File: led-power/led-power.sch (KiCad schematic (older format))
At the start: 97 parts, among them J1 String1, J10 PowerInput, J11 Qwiic, J12 Qwiic, J13 A0, J14 A1, J15 A2, J2 String2, J3 String3, J4 String4, J5 String5, J6 String6, J7 String7, J8 String8, J9 PowerInput, Q1 Q_NMOS_GDS, Q2 Q_NMOS_GDS, Q3 Q_NMOS_GDS, Q4 Q_NMOS_GDS, Q5 Q_NMOS_GDS, Q6 Q_NMOS_GDS, Q7 Q_NMOS_GDS, Q8 Q_NMOS_GDS, U1 MCP6V51, U10 L78L05ACZ-AP, U11 MCP1501, U2 MCP6V51, U3 MCP6V51, U4 MCP6V51, U5 MCP6V51, U6 MCP6V51, U7 MCP6V51, U8 MCP6V51, U9 MCP23017_SO

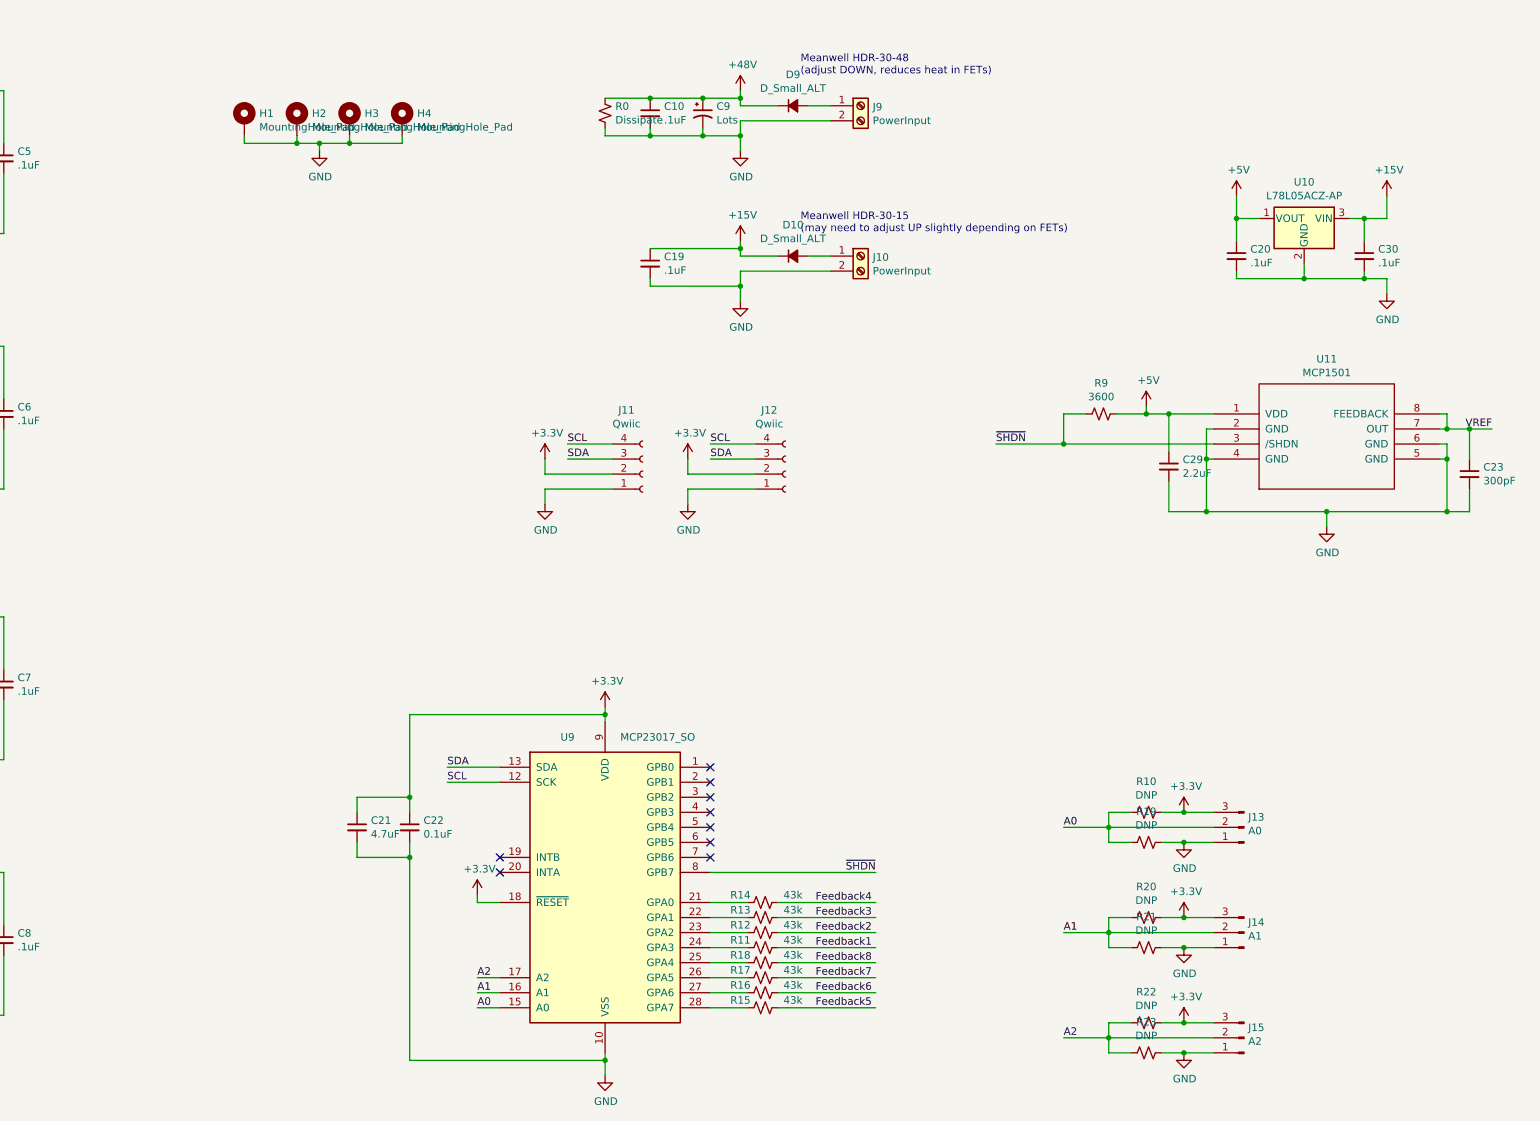
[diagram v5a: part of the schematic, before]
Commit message: Rev 2 changes
* Pulldown on VREF so that ~SHDN can work
* Voltage dividers on the rails, fed to the MCP23017 so it can detect faults
* Increased space between Qwiic headers
* Bring I2C bus out on 0.100" header
* Tweaked LED positions on the left side; right seemed to be fine.
* Converted it to a four layer board. +15V/GND/GND/+48V
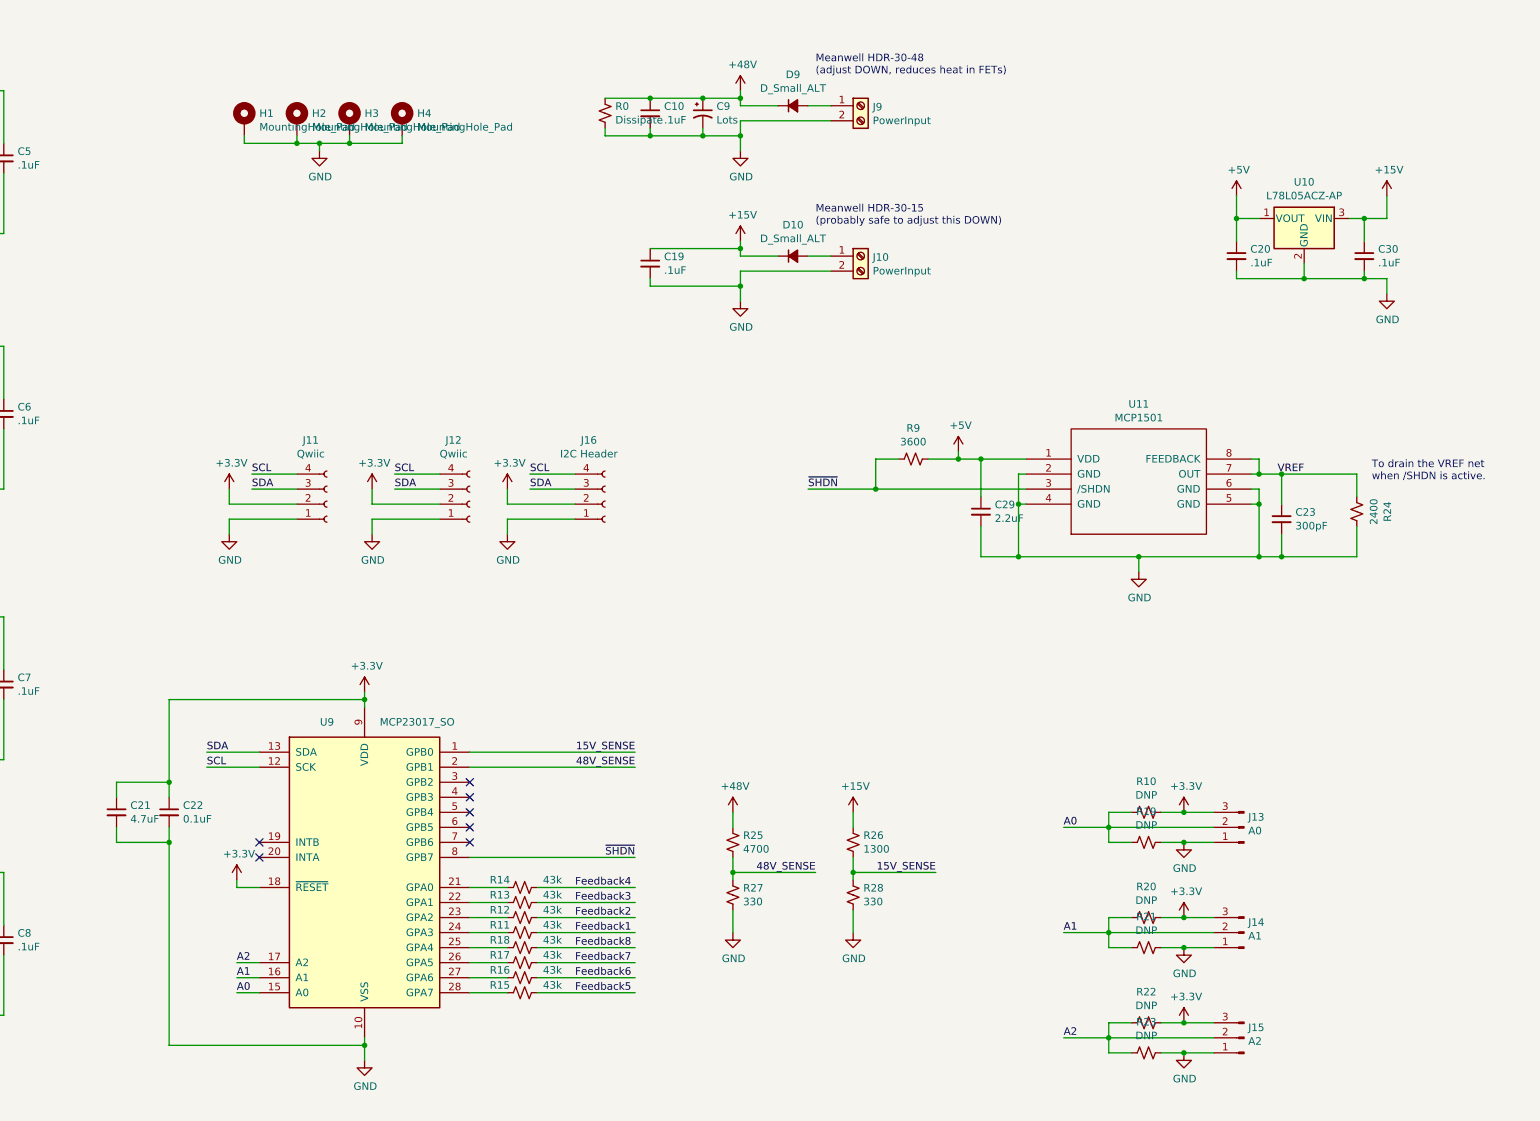
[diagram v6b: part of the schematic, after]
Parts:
- added J16: I2C Header, Pin_Headers:Pin_Header_Straight_1x04_Pitch2.54mm, symbol Connector:Conn_01x04_Female
- added R24: 2400, Resistors_SMD:R_0805_HandSoldering, symbol Device:R_Small_US
- added R25: 4700, Resistors_SMD:R_0805_HandSoldering, symbol Device:R_Small_US
- added R26: 1300, Resistors_SMD:R_0805_HandSoldering, symbol Device:R_Small_US
- added R27, R28: 330, Resistors_SMD:R_0805_HandSoldering, symbol Device:R_Small_US
- H1, H2, H3, H4: footprint Mounting_Holes:MountingHole_3.2mm_M3_Pad -> Mounting_Holes:MountingHole_3.2mm_M3_Pad_Via
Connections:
- net +15V: now also R26.1
- net +3V3: now also J16.2 (Pin_2)
- net +48V: now also R25.1
- net GND: now also J16.1 (Pin_1), R24.1, R27.2, R28.2
- net SCL: now also J16.4 (Pin_4)
- net SDA: now also J16.3 (Pin_3)
- net VREF: now also R24.2
- net 15V_SENSE: now reaches U9.1 (GPB0)
- net 15V_SENSE: now also R26.2, R28.1
- net 48V_SENSE: now reaches U9.2 (GPB1)
- net 48V_SENSE: now also R25.2, R27.1
- no-connect marks 9 -> 7
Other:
- note added: "Meanwell HDR-30-15\n(probably safe to adjust this DOWN)"
- note added: "To drain the VREF net\nwhen /SHDN is active."
- note removed: "Meanwell HDR-30-15\n(may need to adjust UP slightly depending on FETs)"
- moved on the sheet: C21, C22, C23, C29, J11, J12, R11, R12, R13, R14, R15, R16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

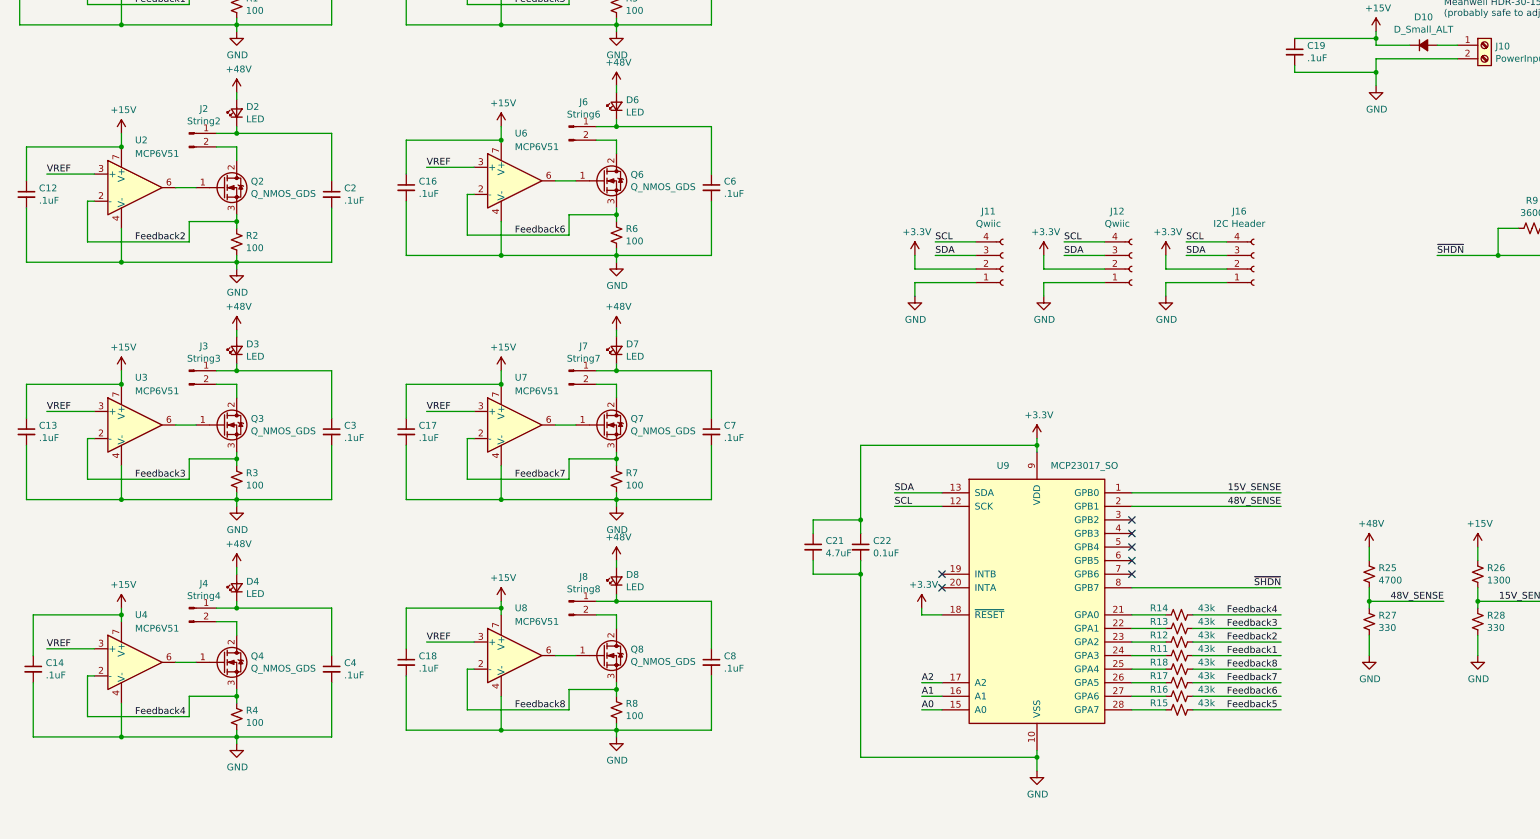
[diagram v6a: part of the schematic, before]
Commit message: Add ~IRQ header, lots of trace cleanup. Bump the board rev
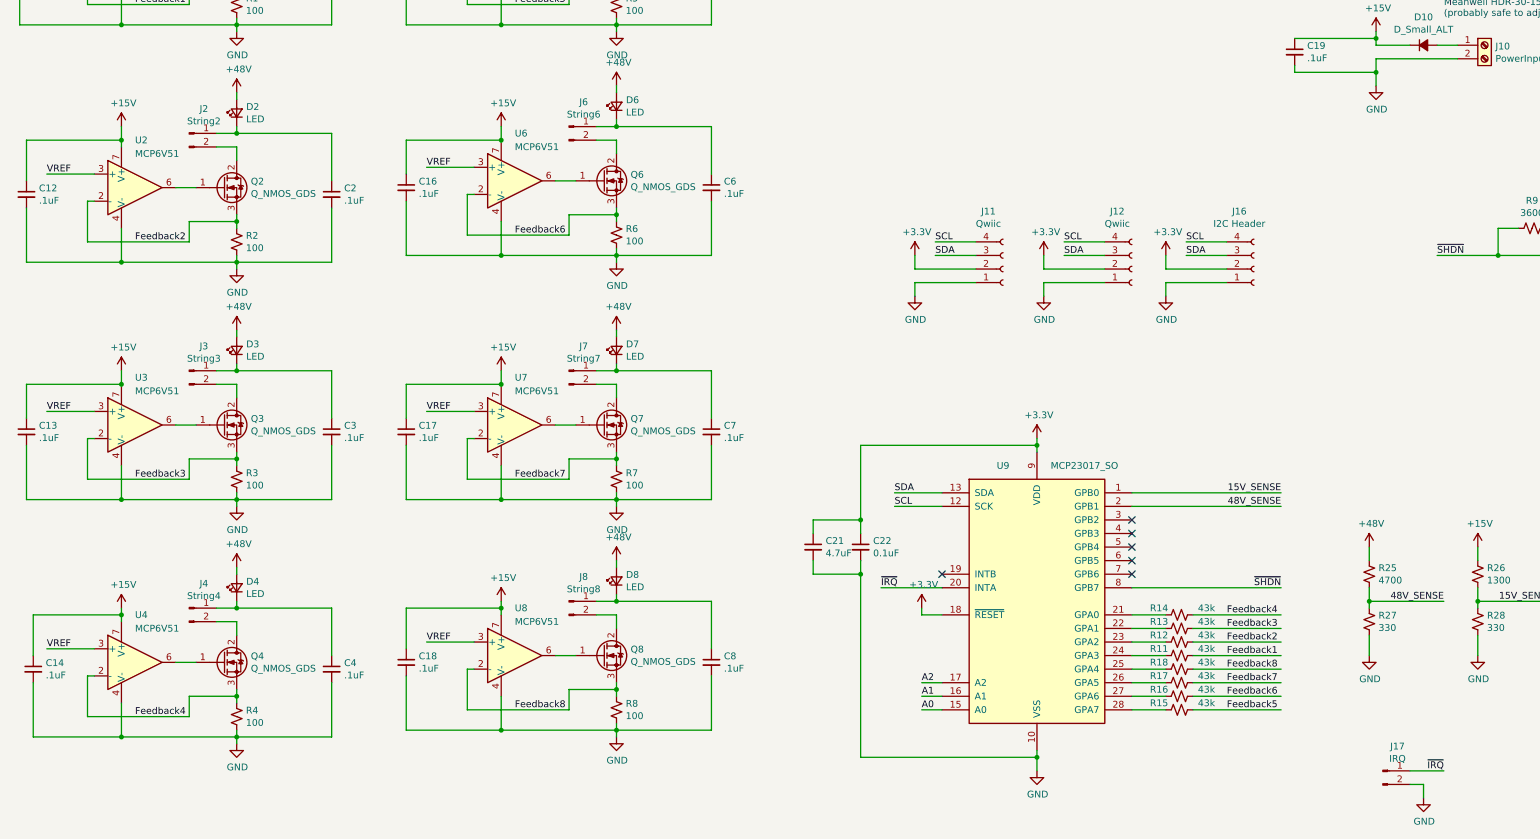
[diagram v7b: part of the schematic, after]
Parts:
- added J17: IRQ, Pin_Headers:Pin_Header_Straight_1x02_Pitch2.54mm, symbol Connector:Conn_01x02_Male
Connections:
- net GND: now also J17.2 (Pin_2)
- net ~IRQ: now reaches U9.20 (INTA)
- net ~IRQ: now also J17.1 (Pin_1)
- no-connect marks 7 -> 6
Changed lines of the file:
@@
 Wire Wire Line
 	2300 3850 2300 3800
-Wire Wire Line
-	1450 2900 1450 3000
 $Comp
 L Device:C_Small C2
@@
 L power:+15V #PWR0120
 U 1 1 5FC5B32C
-P 1450 2900
-F 0 "#PWR0120" H 1450 2750 50  0001 C CNN
-F 1 "+15V" H 1465 3073 50  0000 C CNN
-F 2 "" H 1450 2900 50  0001 C CNN
-F 3 "" H 1450 2900 50  0001 C CNN
-	1    1450 2900
+P 1450 2850
+F 0 "#PWR0120" H 1450 2700 50  0001 C CNN
+F 1 "+15V" H 1465 3023 50  0000 C CNN
+F 2 "" H 1450 2850 50  0001 C CNN
+F 3 "" H 1450 2850 50  0001 C CNN
+	1    1450 2850
 	1    0    0    -1
 $EndComp
@@
 	1    0    0    -1
 $EndComp
-Wire Wire Line
-	750  3250 750  3000
-Wire Wire Line
-	750  3000 1450 3000
-Connection ~ 1450 3000
 Wire Wire Line
 	1450 4750 750  4750
@@
 $EndComp
 NoConn ~ 7500 6150
-NoConn ~ 7500 6250
 $Comp
 L power:GND #PWR0137
@@
 Text Notes 14900 3750 0    50   ~ 0
 To drain the VREF net\nwhen /SHDN is active.
+Wire Wire Line
+	1450 2950 750  2950
+Wire Wire Line
+	750  2950 750  3250
+Wire Wire Line
+	1450 3000 1450 2950
+Wire Wire Line
+	1450 2950 1450 2850
+Connection ~ 1450 2950
+$Comp
+L Connector:Conn_01x02_Male J17
+U 1 1 6027517F
+P 10750 7600
+F 0 "J17" H 10858 7781 50  0000 C CNN
+F 1 "IRQ" H 10858 7690 50  0000 C CNN
+F 2 "Pin_Headers:Pin_Header_Straight_1x02_Pitch2.54mm" H 10750 7600 50  0001 C CNN
+F 3 "~" H 10750 7600 50  0001 C CNN
+	1    10750 7600
+	1    0    0    -1
+$EndComp
+$Comp
+L power:GND #PWR0154
+U 1 1 60277C7E
+P 11050 7800
+F 0 "#PWR0154" H 11050 7550 50  0001 C CNN
+F 1 "GND" H 11055 7627 50  0000 C CNN
+F 2 "" H 11050 7800 50  0001 C CNN
+F 3 "" H 11050 7800 50  0001 C CNN
+	1    11050 7800
+	1    0    0    -1
+$EndComp
+Wire Wire Line
+	10950 7700 11050 7700
+Wire Wire Line
+	11050 7700 11050 7800
+Wire Wire Line
+	10950 7600 11200 7600
+Text Label 11200 7600 2    50   ~ 0
+~IRQ
+Wire Wire Line
+	7500 6250 7050 6250
+Text Label 7050 6250 0    50   ~ 0
+~IRQ
 $EndSCHEMATC
